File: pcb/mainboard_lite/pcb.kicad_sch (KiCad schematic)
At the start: 0 parts

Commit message: Lite version r0p1
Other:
- added sheet mcu (mcu.kicad_sch)
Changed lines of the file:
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@@
     (instances
       (project "pcb"
-        (path "/4654897e-3e2f-4522-96c3-20b19803c088" (page "7"))
+        (path "/4654897e-3e2f-4522-96c3-20b19803c088" (page "5"))
       )
     )
@@
     (instances
       (project "pcb"
-        (path "/4654897e-3e2f-4522-96c3-20b19803c088" (page "5"))
+        (path "/4654897e-3e2f-4522-96c3-20b19803c088" (page "4"))
       )
     )
@@
       )
     )
+  )
+  (sheet (at 33.02 85.09) (size 53.34 6.35) (fields_autoplaced)
+    (stroke (width 0.1524) (type solid))
+    (fill (color 0 0 0 0.0000))
+    (property "Sheetname" "mcu" (at 33.02 84.3784 0)
+      (effects (font (size 1.27 1.27)) (justify left bottom))
+    )
+    (property "Sheetfile" "mcu.kicad_sch" (at 33.02 92.0246 0)
+      (effects (font (size 1.27 1.27)) (justify left top))
+    )
+    (instances
+      (project "pcb"
+        (path "/4654897e-3e2f-4522-96c3-20b19803c088" (page "6"))
+      )
+    )

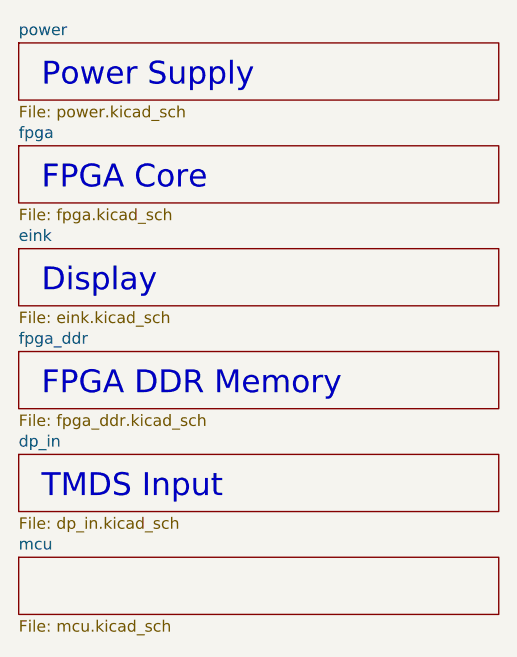
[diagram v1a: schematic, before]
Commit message: lite r0p1 schematic fixes
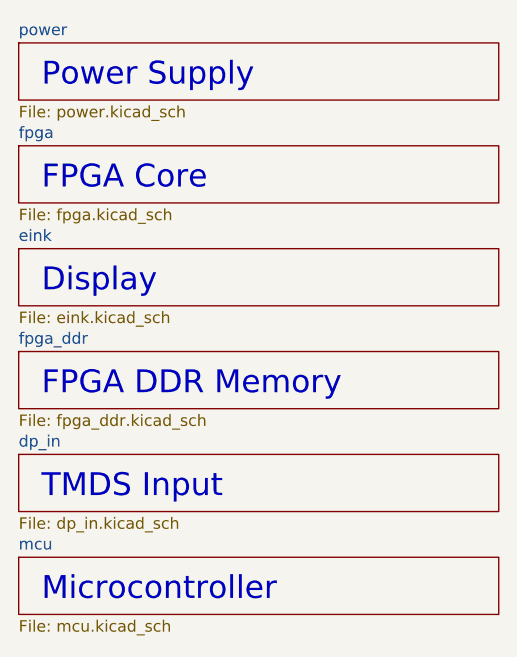
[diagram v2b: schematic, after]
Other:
- note added: "Microcontroller"
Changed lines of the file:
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@@
+    (effects (font (size 2.54 2.54)) (justify left bottom))
+  )
+  (text "Microcontroller" (at 35.56 90.17 0)
     (effects (font (size 2.54 2.54)) (justify left bottom))
   )
